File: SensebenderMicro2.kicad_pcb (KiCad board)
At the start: 2 copper layers, 21.5 x 32 mm, 95 parts, among them P2 MYSX_2.4, P3 Antenna, U1 ATSAMD21E, U2 MCP1703T-3302E, U3 NRF24L01, U4 RFM69HW, U5 ATSHA204A, U6 AT45DB041E, U7 Si7021, U8 AT24C32-STUM-T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

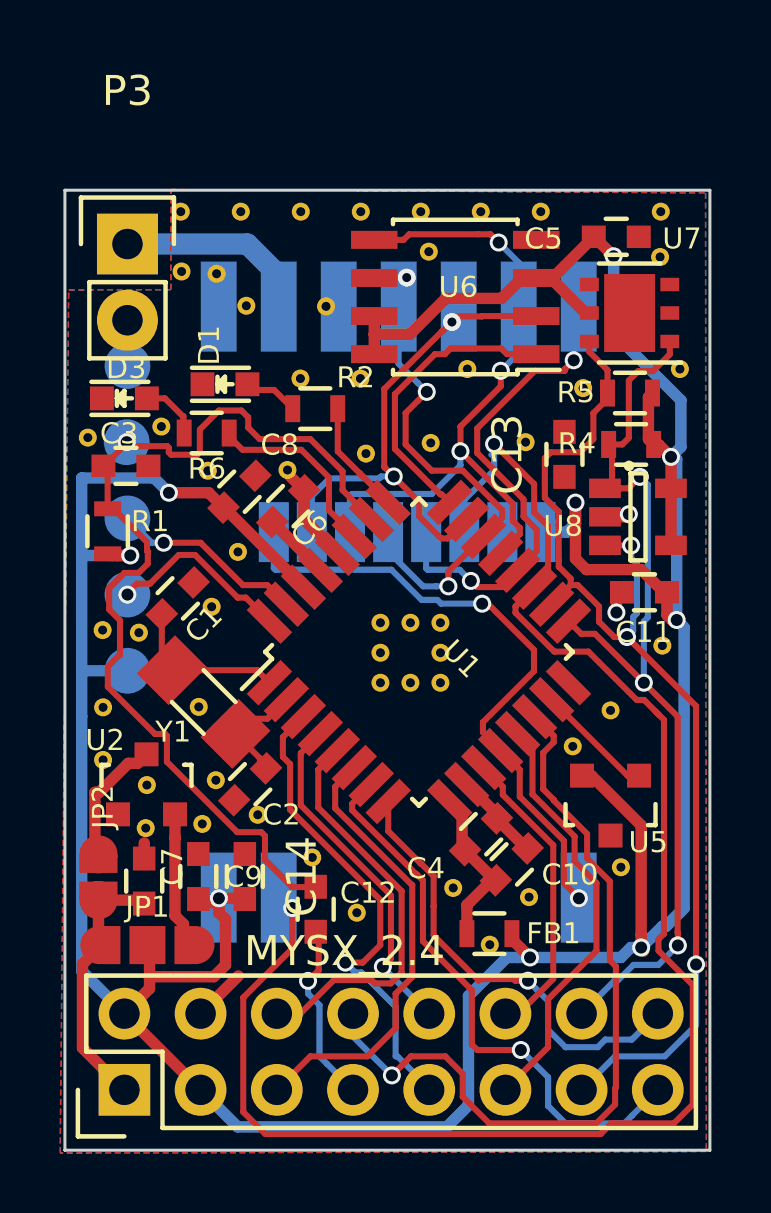
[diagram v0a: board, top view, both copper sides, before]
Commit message: Changed to use RFM69HCW footprint (compatible with RFM95)
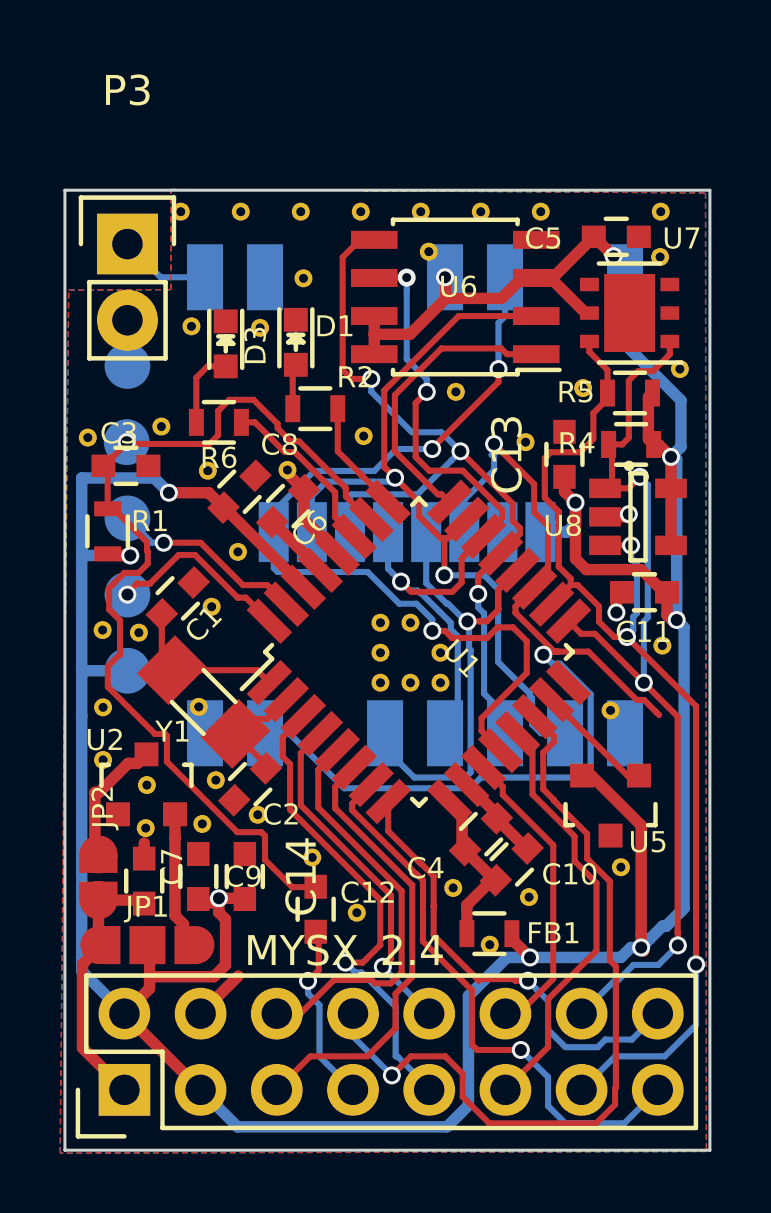
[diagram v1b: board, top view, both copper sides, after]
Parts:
- removed the REF** at (105.9, 100.5)
- removed the REF** at (101.2, 90.4)
- removed the REF** at (97.7, 85.9)
- removed the REF** at (99.0, 90.8)
- removed the REF** at (98.9, 88.3)
- removed the REF** at (96.9, 88.3)
- removed the REF** at (92.9, 84.7)
- removed the REF** at (101.5, 96.4)
- removed the REF** at (94.1, 84.8)
- removed the REF** at (95.0, 85.9)
- added REF**: via-0.6mm, mysensors_obscurities:via-0.6mm, F.Cu at (95.5, 86.6)
- added REF**: via-0.6mm, mysensors_obscurities:via-0.6mm, F.Cu at (93.2, 86.5)
- added REF**: via-0.6mm, mysensors_obscurities:via-0.6mm, F.Cu at (97.0, 84.9)
- added REF**: via-0.6mm, mysensors_obscurities:via-0.6mm, F.Cu at (99.0, 90.2)
- U1: value ATSAMD21E -> ATSAMD20E
- U4: footprint mysensors_radios:RFM69HW_SMD_Handsoldering -> mysensors_radios:RFM95HW_SMD
- U8: value AT24C32-STUM-T -> 24AA32AT-I/OT
- moved U4 5.10 mm to (107.7, 99.1)
- moved D3 3.84 mm to (94.4, 87.1), turned to 270 degrees
- moved D1 2.74 mm to (96.7, 87.1), turned to 270 degrees
- moved REF** 0.85 mm to (102.0, 88.7)
- moved R6 0.54 mm to (94.1, 89.7)
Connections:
- P3 pad 1: Net-(P3-Pad1) -> /ANT
- U4 pad 1: Net-(U4-Pad1) -> GND
- U4 pad 10: Net-(P3-Pad1) -> GND
- U4 pad 11: GND -> Net-(U4-Pad11)
- U4 pad 12: /SCK -> Net-(U4-Pad12)
- U4 pad 13: /MISO -> +3V3
- U4 pad 14: /MOSI -> /IRQ
- U4 pad 15: /CSN -> Net-(U4-Pad15)
- U4 pad 2: /IRQ -> /MISO
- U4 pad 3: Net-(U4-Pad3) -> /MOSI
- U4 pad 4: Net-(U4-Pad4) -> /SCK
- U4 pad 5: Net-(U4-Pad5) -> /CSN
- U4 pad 8: +3V3 -> GND
- U4 pad 9: GND -> /ANT
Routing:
- net /NRF_CE_RFM_DIO5: track 54.0 -> 33.7 mm
- net /MISO: track 17.4 -> 26.6 mm
- net /IRQ: track 21.7 -> 29.7 mm, vias 2 -> 3
- net /SCK: track 17.1 -> 24.4 mm
- net Net-(U4-Pad16): track 0.00 -> 7.29 mm, vias 0 -> 1
- net Net-(P3-Pad1): track 6.54 -> 0.00 mm
- net +3V3: track 125.4 -> 119.8 mm
- net /ANT: track 0.00 -> 3.04 mm
- net /MOSI: track 24.0 -> 27.0 mm
- net /CSN: track 17.3 -> 15.5 mm, vias 2 -> 1
- net Net-(D3-Pad2): track 2.12 -> 2.62 mm

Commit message: Updated layout a bit
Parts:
- removed the REF** at (91.5, 96.7)
- removed the REF** at (90.3, 96.7)
- removed the REF** at (91.7, 103.3)
- JP1, JP2: moved to B.Cu
- moved C3 2.51 mm to (91.5, 88.7)
- moved R1 2.27 mm to (91.1, 91.2), turned to 180 degrees
- moved U2 1.92 mm to (91.2, 103.7)
- moved C14 1.32 mm to (94.4, 106.0), turned to 180 degrees
- moved C9 1.19 mm to (94.6, 104.5), turned to 180 degrees
- moved C7 1.05 mm to (91.4, 106.0), turned to 0 degrees
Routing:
- net /RESET: track 32.6 -> 14.6 mm
- net Net-(U4-Pad16): track 7.29 -> 0.00 mm, vias 1 -> 0
- net GND: track 10.3 -> 14.8 mm
- net Net-(JP2-Pad2): track 4.36 -> 2.44 mm, vias 0 -> 1
- net +3V3: track 119.8 -> 121.4 mm
- net Net-(JP1-Pad1): track 4.48 -> 3.22 mm, vias 0 -> 1
- net /V_RAW: track 8.88 -> 8.57 mm, vias 0 -> 1
